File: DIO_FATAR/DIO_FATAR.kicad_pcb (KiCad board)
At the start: 2 copper layers, 100 x 50 mm, 20 parts, among them J1 in, J2 thru, J3 right, J4 left, U1 74HC595, U2 74HC595, U3 74165, U4 74165

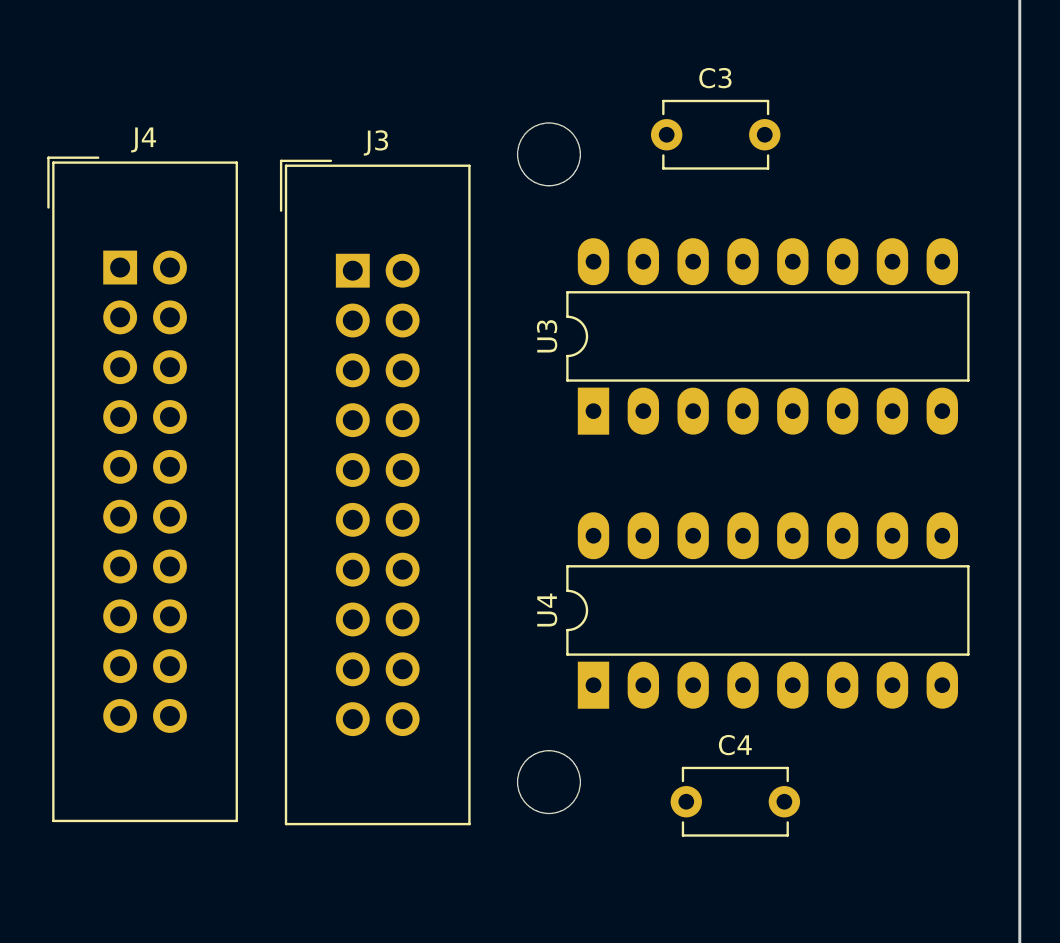
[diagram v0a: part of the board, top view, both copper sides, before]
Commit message: DIO_FATAR: route input sr
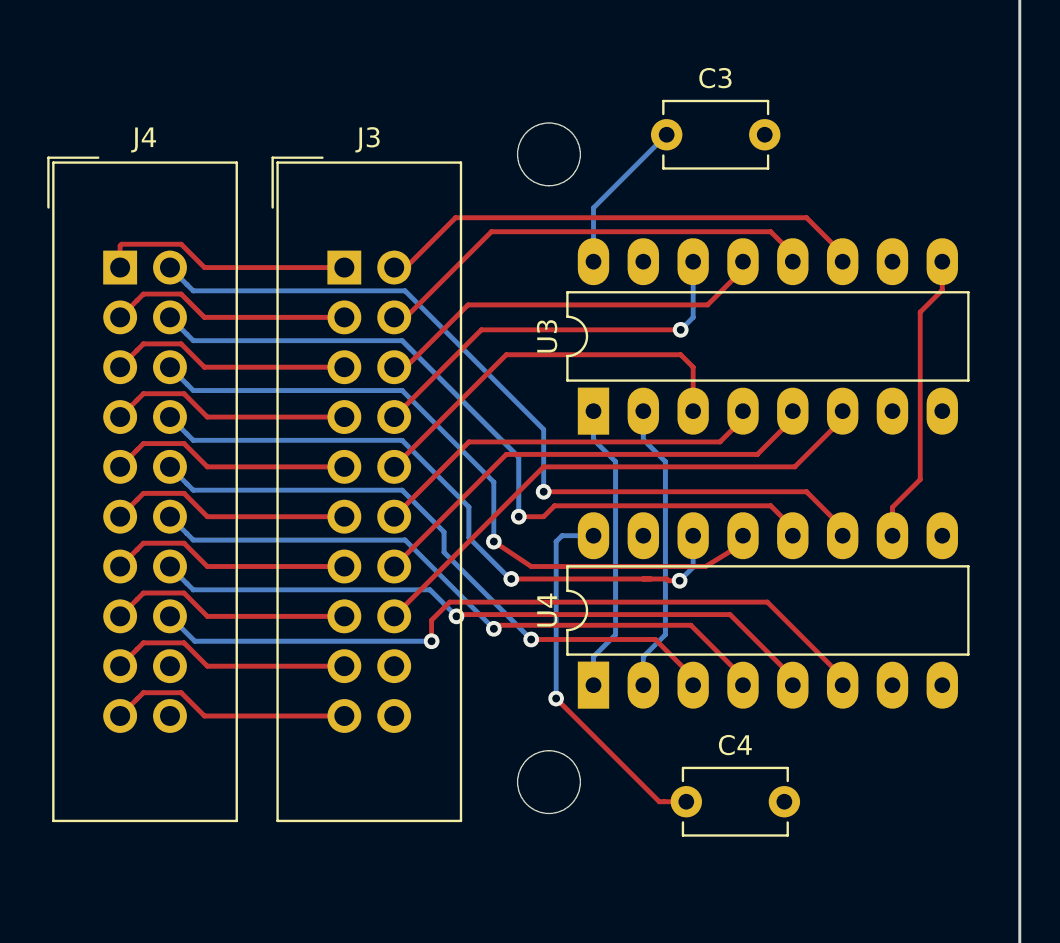
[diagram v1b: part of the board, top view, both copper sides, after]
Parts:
- moved J3 0.46 mm to (115.6, 64.8)
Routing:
- net /T_L_0: track 0.00 -> 42.0 mm, vias 0 -> 1
- net /T_L_1: track 0.00 -> 38.8 mm, vias 0 -> 1
- net /T_L_7: track 0.00 -> 38.3 mm, vias 0 -> 1
- net /T_L_2: track 0.00 -> 35.8 mm, vias 0 -> 1
- net /T_L_6: track 0.00 -> 34.6 mm, vias 0 -> 1
- net /T_L_3: track 0.00 -> 33.7 mm, vias 0 -> 2
- net /T_L_5: track 0.00 -> 33.2 mm, vias 0 -> 1
- net /T_L_4: track 0.00 -> 32.1 mm, vias 0 -> 1
- net /T_R_7: track 0.00 -> 27.4 mm
- net +5V: track 0.00 -> 27.3 mm, vias 0 -> 1
- net /T_R_0: track 0.00 -> 24.7 mm
- net /T_R_6: track 0.00 -> 23.8 mm
- net /T_R_1: track 0.00 -> 22.6 mm
- net /T_R_5: track 0.00 -> 20.2 mm
- net /T_R_3: track 0.00 -> 20.2 mm, vias 0 -> 1
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
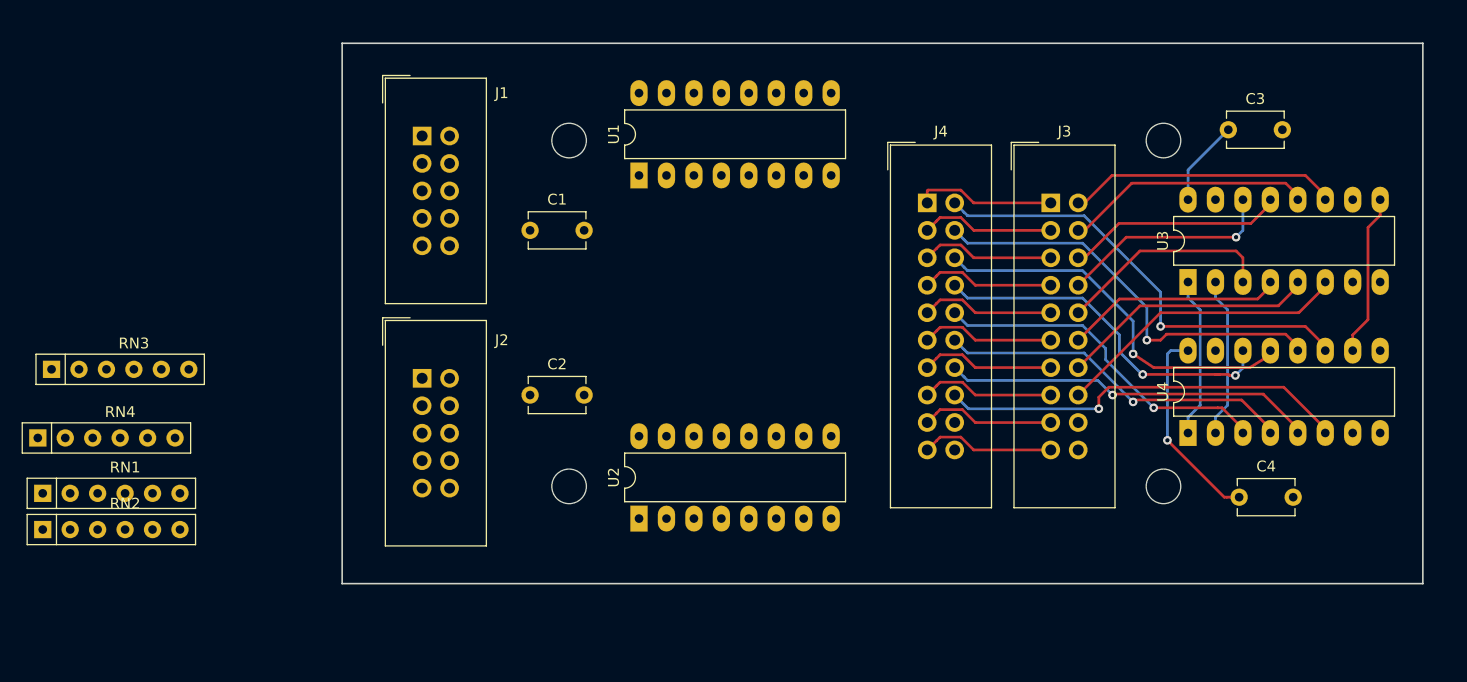
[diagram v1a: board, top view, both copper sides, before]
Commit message: DIO_FATAR: move J1,2 for better clock routing
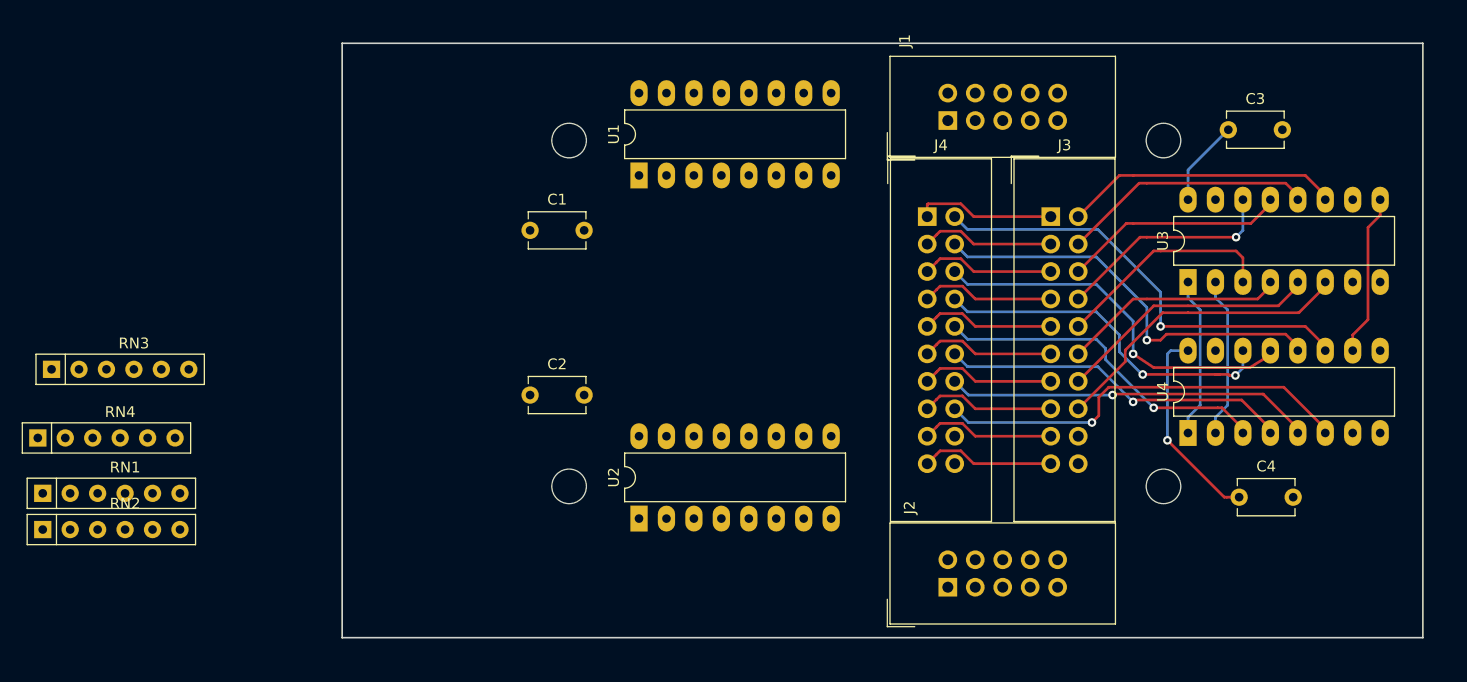
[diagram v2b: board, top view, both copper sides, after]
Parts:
- moved J2 52.3 mm to (106.0, 100.3), turned to 90 degrees
- moved J1 48.7 mm to (106.0, 57.1), turned to 90 degrees
- moved J3 1.27 mm to (115.6, 66.0)
- moved J4 1.27 mm to (104.1, 66.0)
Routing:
- net /T_R_7: track 27.4 -> 28.6 mm
- net /T_L_7: track 38.3 -> 39.2 mm
- net /T_R_2: track 19.9 -> 20.8 mm
- net /T_R_1: track 22.6 -> 23.5 mm
- net /T_R_0: track 24.7 -> 25.6 mm
- net /T_L_6: track 34.6 -> 33.9 mm
- net /T_L_0: track 42.0 -> 41.5 mm
- net /T_L_2: track 35.8 -> 35.3 mm
- net /T_L_4: track 32.1 -> 31.6 mm
- net /T_R_4: track 20.1 -> 20.6 mm
- net /T_R_3: track 20.2 -> 20.7 mm
- net /T_L_5: track 33.2 -> 32.6 mm
- net /T_L_1: track 38.8 -> 38.3 mm
- net /T_R_6: track 23.8 -> 24.4 mm
- net /T_R_5: track 20.2 -> 20.8 mm
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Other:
- board size 100 x 50 mm -> 100 x 55 mm

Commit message: DIO_FATAR: position resistor networks
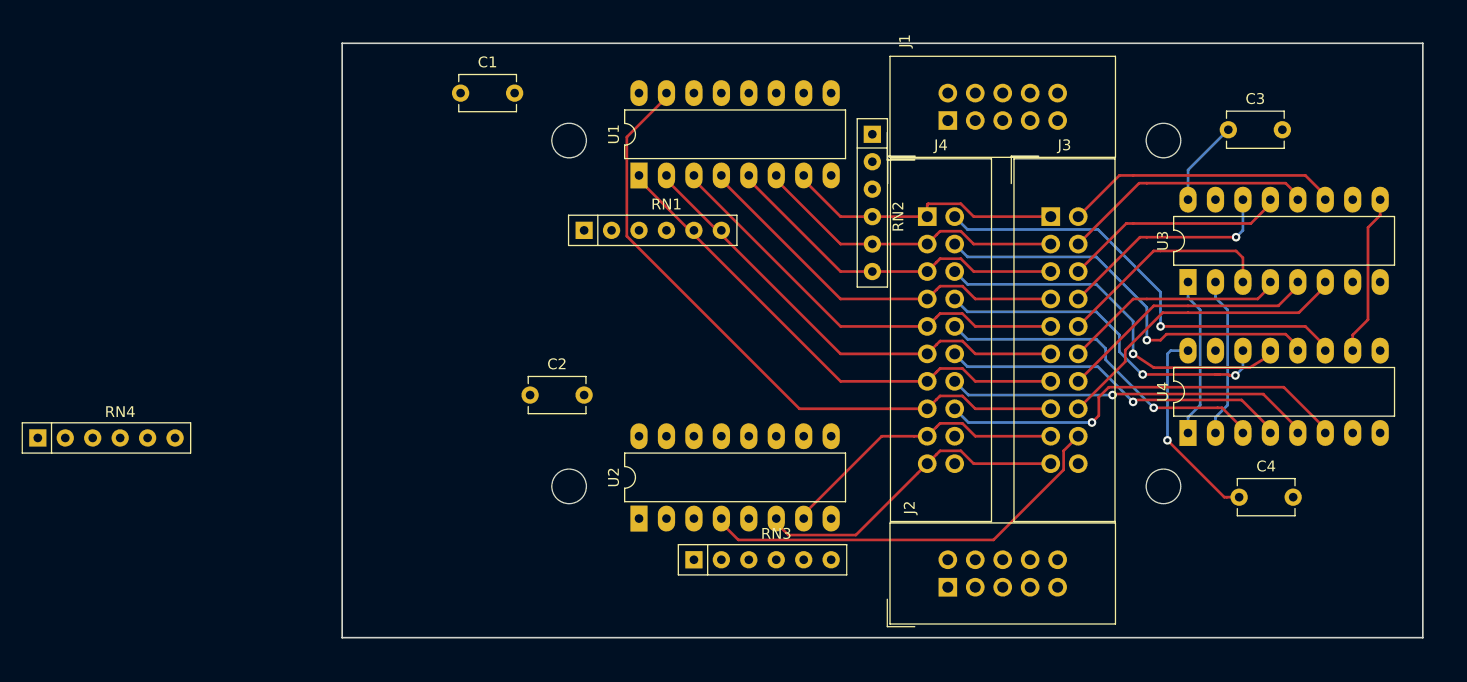
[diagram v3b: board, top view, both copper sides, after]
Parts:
- moved RN2 85.0 mm to (99.1, 58.4), turned to 270 degrees
- moved RN3 62.0 mm to (82.5, 97.8)
- moved RN1 55.7 mm to (72.4, 67.3)
- moved C1 14.2 mm to (61.0, 54.6)
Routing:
- net /BK_3_8: track 12.4 -> 61.6 mm
- net /BK_10: track 0.00 -> 39.1 mm
- net /MK_3_8: track 12.4 -> 47.2 mm
- net /BK_2_7: track 12.4 -> 43.6 mm
- net /MK_2_7: track 12.4 -> 40.0 mm
- net /BK_1_6: track 12.4 -> 36.4 mm
- net /MK_1_6: track 12.4 -> 32.8 mm
- net /BK_4_9: track 12.4 -> 30.0 mm
- net /BK_0_5: track 12.4 -> 29.2 mm
- net /MK_4_9: track 12.4 -> 27.2 mm
- net /MK_0_5: track 13.1 -> 26.3 mm

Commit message: DIO_FATAR: connect and roughly position resistor networks
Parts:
- moved RN4 90.0 mm to (111.8, 90.2), turned to 90 degrees
- moved RN1 51.8 mm to (123.2, 57.1), turned to 270 degrees
- moved RN3 46.0 mm to (111.8, 62.2), turned to 270 degrees
- moved RN2 36.9 mm to (123.2, 86.4), turned to 90 degrees
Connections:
- RN1 pad 2: Net-(RN1-Pad2) -> /SI_THRU
- RN1 pad 3: Net-(RN1-Pad3) -> /T_R_0
- RN1 pad 4: Net-(RN1-Pad4) -> /T_R_1
- RN1 pad 5: Net-(RN1-Pad5) -> /T_R_2
- RN1 pad 6: Net-(RN1-Pad6) -> /T_R_3
- RN2 pad 3: Net-(RN2-Pad3) -> /T_R_7
- RN2 pad 4: Net-(RN2-Pad4) -> /T_R_6
- RN2 pad 5: Net-(RN2-Pad5) -> /T_R_5
- RN2 pad 6: Net-(RN2-Pad6) -> /T_R_4
- RN3 pad 3: Net-(RN3-Pad3) -> /T_L_0
- RN3 pad 4: Net-(RN3-Pad4) -> /T_L_1
- RN3 pad 5: Net-(RN3-Pad5) -> /T_L_2
- RN3 pad 6: Net-(RN3-Pad6) -> /T_L_3
- RN4 pad 3: Net-(RN4-Pad3) -> /T_L_7
- RN4 pad 4: Net-(RN4-Pad4) -> /T_L_6
- RN4 pad 5: Net-(RN4-Pad5) -> /T_L_5
- RN4 pad 6: Net-(RN4-Pad6) -> /T_L_4
- U3 pad 9: Net-(U3-Pad9) -> Net-(RN3-Pad2)
- U4 pad 10: Net-(U3-Pad9) -> Net-(RN3-Pad2)
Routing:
- net Net-(U3-Pad9): track 15.0 -> 0.00 mm
- net Net-(RN3-Pad2): track 0.00 -> 15.0 mm
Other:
- net class Power added: clearance 0.2, trace_width 0.5, via_dia 1, via_drill 0.6

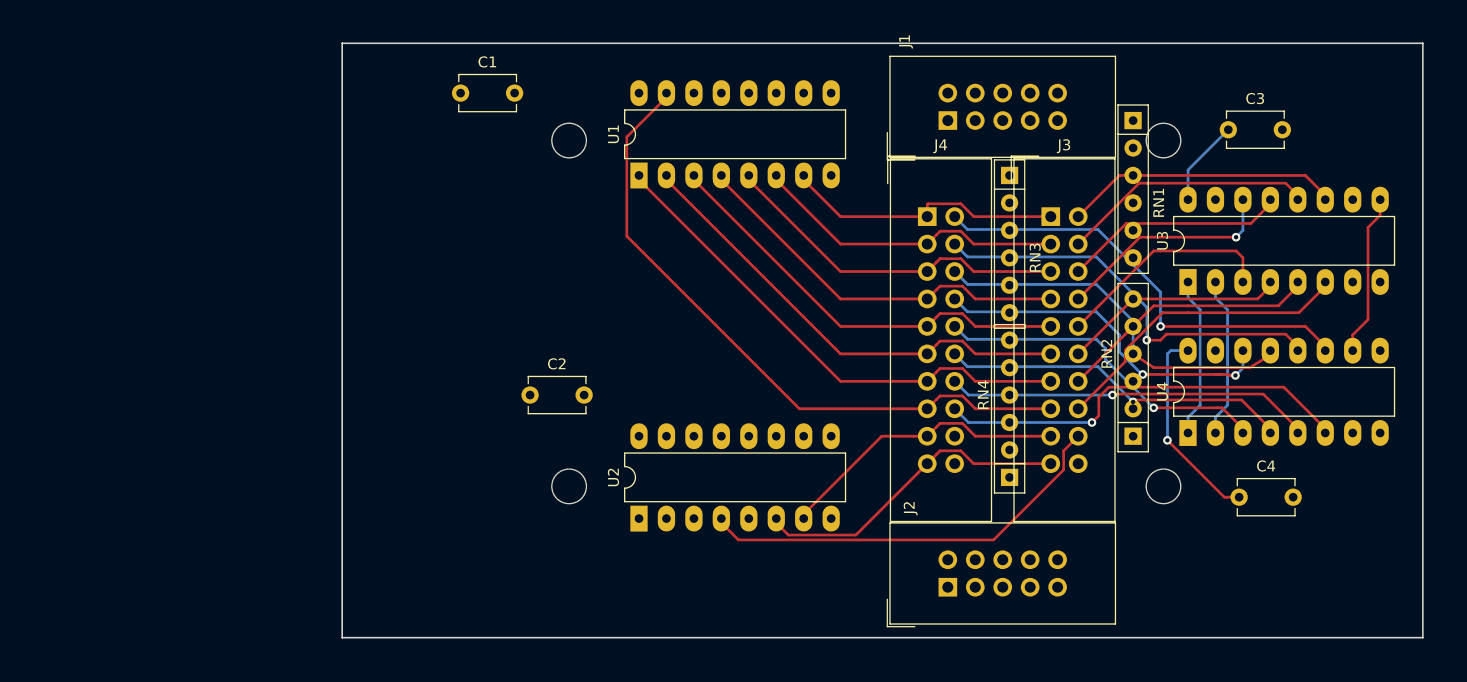
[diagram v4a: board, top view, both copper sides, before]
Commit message: DIO_FATAR: route everything except two resistors
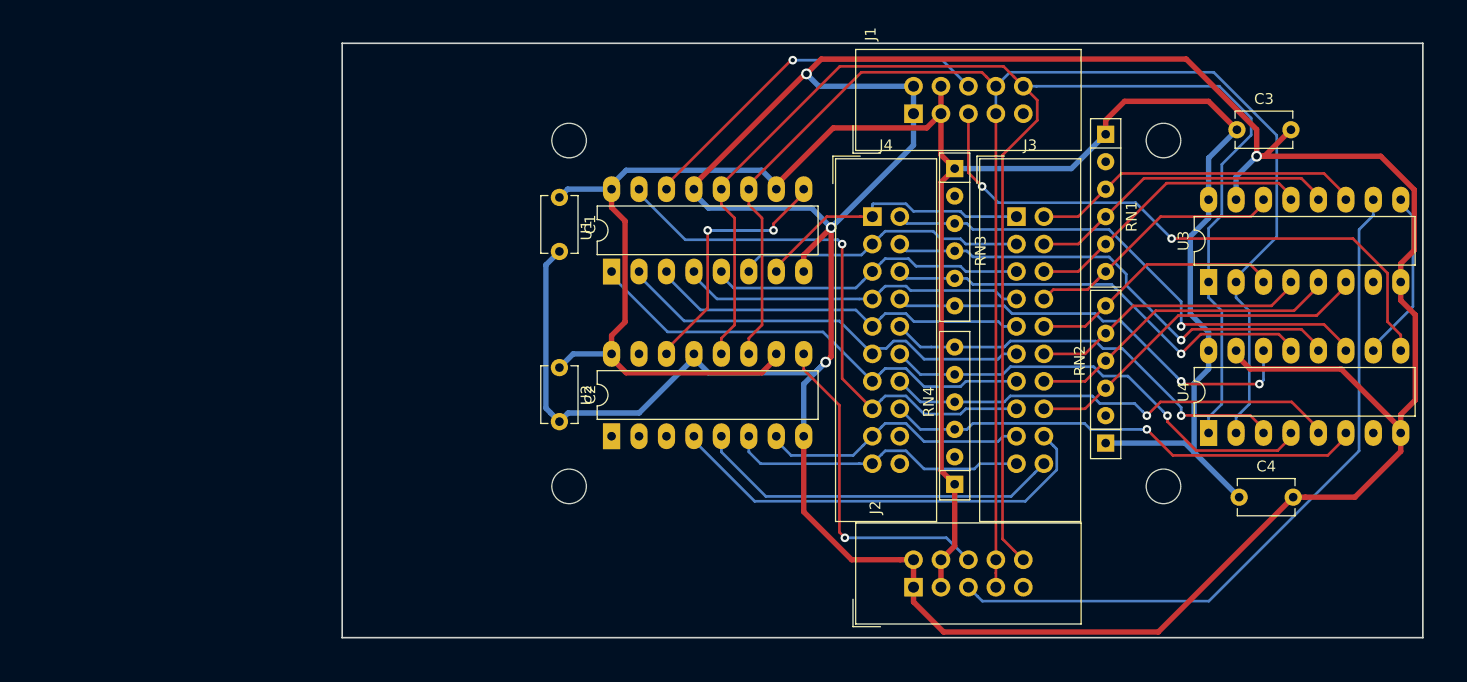
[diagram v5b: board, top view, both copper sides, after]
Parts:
- moved C1 13.3 mm to (70.1, 64.3), turned to 270 degrees
- moved U1 9.25 mm to (74.9, 71.1)
- moved U2 8.03 mm to (74.9, 86.4)
- moved RN4 5.12 mm to (106.7, 90.8)
- moved RN3 5.12 mm to (106.7, 61.6)
- moved J4 5.08 mm to (99.1, 66.0)
- moved C2 3.72 mm to (70.1, 80.0), turned to 270 degrees
- moved J1 3.24 mm to (102.9, 56.5)
- moved J2 3.17 mm to (102.9, 100.3)
- moved J3 3.17 mm to (112.4, 66.0)
- moved RN1 2.84 mm to (120.7, 58.4)
- moved RN2 2.62 mm to (120.7, 87.0)
- moved U3 1.91 mm to (130.2, 72.1)
- moved U4 1.91 mm to (130.2, 86.1)
- moved C3 0.79 mm to (132.8, 58.0)
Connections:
- RN1 pad 2: /SI_THRU -> Net-(RN1-Pad2)
- RN2 pad 2: Net-(RN2-Pad2) -> /SI_THRU
- U2 pad 16: Net-(U1-Pad9) -> +5V
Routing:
- net GND: track 0.00 -> 320.2 mm, vias 0 -> 4
- net +5V: track 27.3 -> 205.7 mm, vias 1 -> 0
- net /RC: track 14.9 -> 151.7 mm
- net /SC: track 15.7 -> 150.2 mm
- net /SI_THRU: track 0.00 -> 66.2 mm
- net /SI: track 0.00 -> 55.8 mm, vias 0 -> 2
- net /MK_10: track 0.00 -> 34.3 mm
- net /SO: track 0.00 -> 34.1 mm, vias 0 -> 1
- net /SO_THRU: track 0.00 -> 30.9 mm, vias 0 -> 1
- net Net-(U1-Pad9): track 0.00 -> 30.0 mm, vias 0 -> 2
- net /BK_3_8: track 61.6 -> 52.3 mm, vias 0 -> 1
- net /T_L_5: track 32.6 -> 41.7 mm
- net /T_L_6: track 33.9 -> 42.5 mm
- net /T_L_4: track 31.6 -> 38.9 mm
- net /T_R_2: track 20.8 -> 27.5 mm
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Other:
- net class Serial added: clearance 0.3, trace_width 0.25, via_dia 0.8, via_drill 0.4
